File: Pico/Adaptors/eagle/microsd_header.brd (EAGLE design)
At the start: 39.3 x 17.8 mm, 3 parts

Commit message: minor board tweaks
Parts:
- R1: value (none) -> 100k
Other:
- board text added: "Pico this side"
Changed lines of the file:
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@@
 <text x="19.05" y="6.35" size="1.4224" layer="26" rot="MR0">Espruino Pico
 MicroSD rev 1.0</text>
+<text x="2.54" y="12.7" size="1.016" layer="25">Pico this side</text>
 </plain>
 <attributes>
@@
 <elements>
 <element name="J1" library="OPL Eagle Library" package="9P-SMD-W/-RING" value="" x="24.13" y="8.89"/>
-<element name="R1" library="rcl" package="R1206" value="" x="20.32" y="11.43"/>
+<element name="R1" library="rcl" package="R1206" value="100k" x="20.32" y="11.43" smashed="yes">
+<attribute name="NAME" x="19.05" y="12.7" size="1.27" layer="25"/>
+</element>
 <element name="U$1" library="espruino_pico" package="ESPRUINO_PICO_0.1" value="ESPRUINO_PICO_0.1" x="13.97" y="8.89"/>
 </elements>

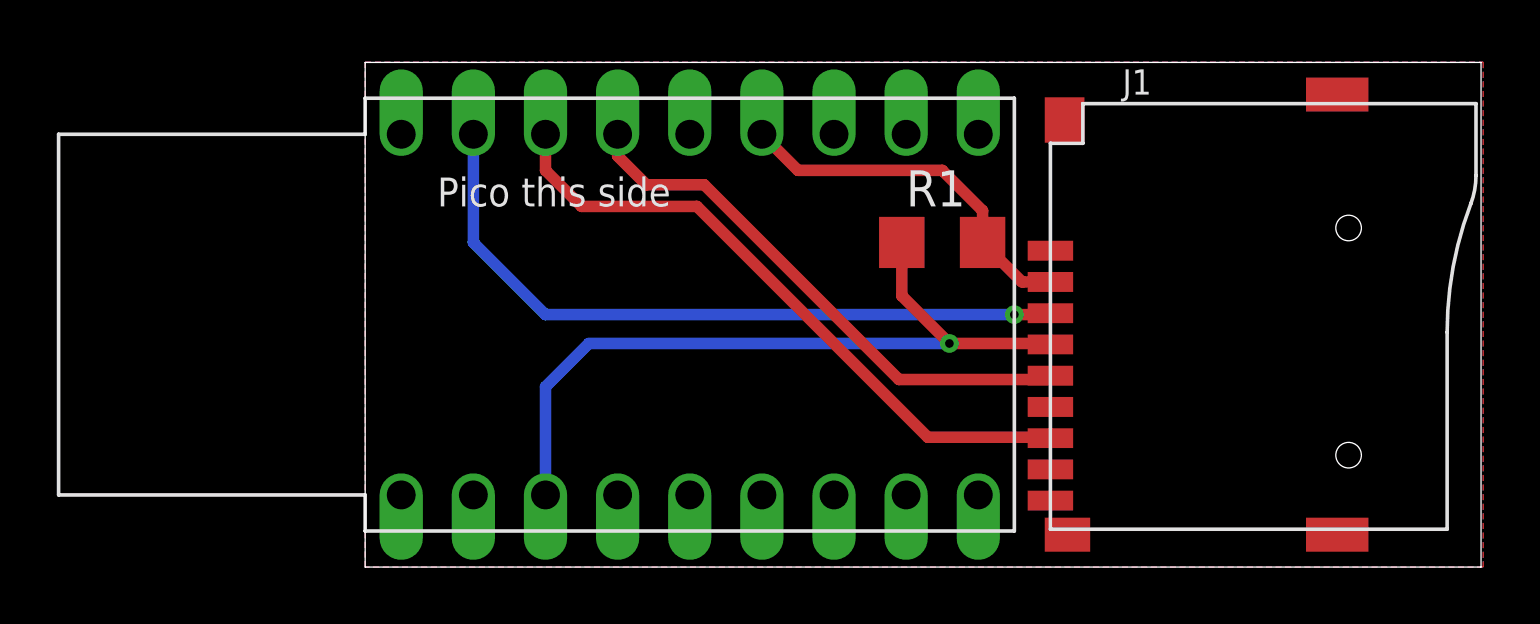
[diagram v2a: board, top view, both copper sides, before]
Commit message: fixes for SD card adaptor
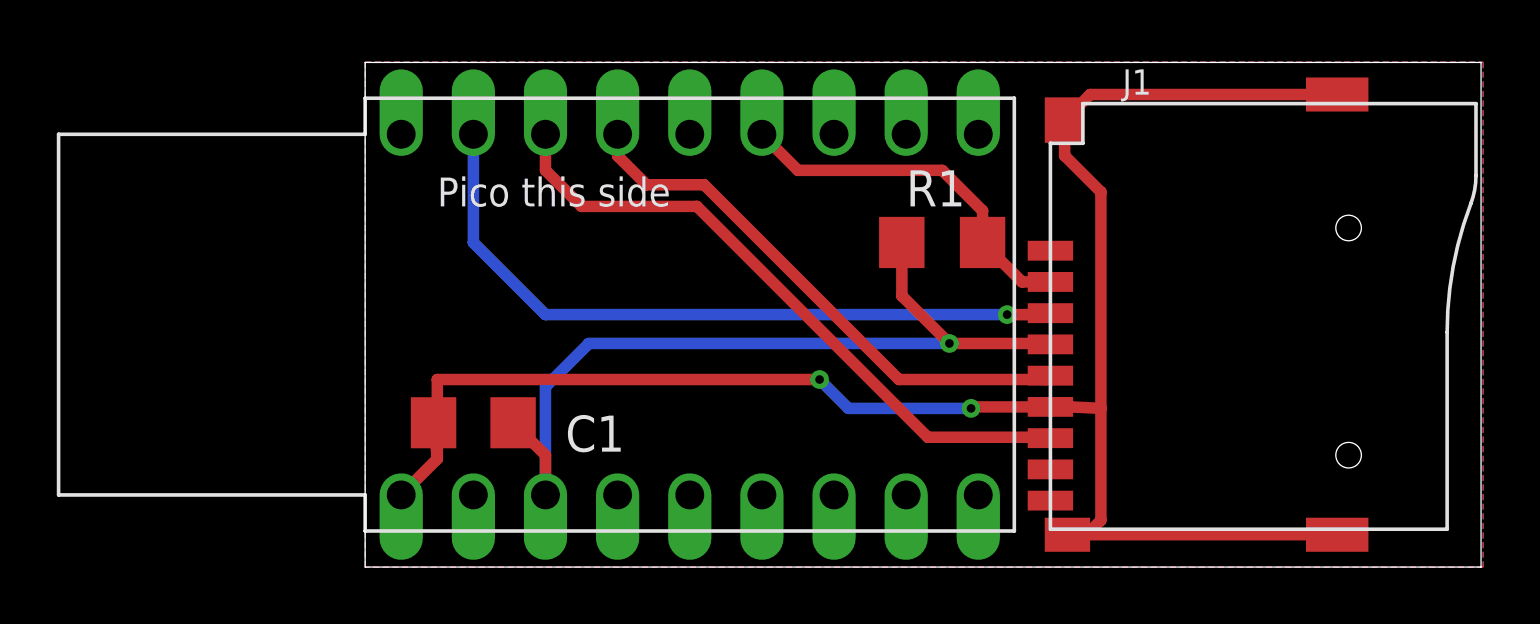
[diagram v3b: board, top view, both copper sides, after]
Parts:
- added C1: 0.1uF, rcl:C1206
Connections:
- removed net N$2: U$1.GND
- new net GND: C1.2, J1.6, J1.G1, J1.G2, J1.G3, J1.G4, U$1.GND
- net 3.3V: now also C1.1
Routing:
- net GND: track 0.00 -> 64.8 mm, vias 0 -> 2
- net 3.3V: track 26.5 -> 29.5 mm
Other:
- board text added: "Espruino Pico MicroSD rev 1.1"
- board text removed: "Espruino Pico MicroSD rev 1.0"
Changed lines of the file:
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@@
 <layers>
 <layer number="1" name="Top" color="4" fill="1" visible="yes" active="yes"/>
+<layer number="2" name="Route2" color="1" fill="3" visible="no" active="no"/>
+<layer number="15" name="Route15" color="4" fill="6" visible="no" active="no"/>
 <layer number="16" name="Bottom" color="1" fill="1" visible="yes" active="yes"/>
 <layer number="17" name="Pads" color="2" fill="1" visible="yes" active="yes"/>
@@
 CS   B1</text>
 <text x="19.05" y="6.35" size="1.4224" layer="26" rot="MR0">Espruino Pico
-MicroSD rev 1.0</text>
+MicroSD rev 1.1</text>
 <text x="2.54" y="12.7" size="1.016" layer="25">Pico this side</text>
 </plain>
@@
 </element>
 <element name="U$1" library="espruino_pico" package="ESPRUINO_PICO_0.1" value="ESPRUINO_PICO_0.1" x="13.97" y="8.89"/>
+<element name="C1" library="rcl" package="C1206" value="0.1uF" x="3.81" y="5.08" smashed="yes" rot="R180">
+<attribute name="NAME" x="9.144" y="5.334" size="1.27" layer="25" rot="R180"/>
+<attribute name="VALUE" x="6.858" y="7.62" size="1.27" layer="27" rot="R180"/>
+</element>
 </elements>
 <signals>
 <signal name="3.3V">
 <contactref element="J1" pad="4"/>
-<contactref element="R1" pad="1"/>
 <contactref element="U$1" pad="3.3V"/>
 <wire x1="24.13" y1="7.84" x2="24.096" y2="7.874" width="0.4064" layer="1"/>
-<wire x1="20.574" y1="7.874" x2="18.898" y2="9.55" width="0.4064" layer="1"/>
-<wire x1="18.898" y1="9.55" x2="18.898" y2="11.43" width="0.4064" layer="1"/>
 <wire x1="6.35" y1="2.54" x2="6.35" y2="6.35" width="0.4064" layer="16"/>
 <wire x1="6.35" y1="6.35" x2="7.874" y2="7.874" width="0.4064" layer="16"/>
@@
 <wire x1="20.574" y1="7.874" x2="24.096" y2="7.874" width="0.4064" layer="1"/>
 <via x="20.574" y="7.874" extent="1-16" drill="0.3048"/>
+<contactref element="C1" pad="1"/>
+<wire x1="6.35" y1="2.54" x2="6.35" y2="3.94" width="0.4064" layer="1"/>
+<wire x1="6.35" y1="3.94" x2="5.21" y2="5.08" width="0.4064" layer="1"/>
+<contactref element="R1" pad="1"/>
+<wire x1="18.898" y1="11.43" x2="18.898" y2="9.55" width="0.4064" layer="1"/>
+<wire x1="18.898" y1="9.55" x2="20.574" y2="7.874" width="0.4064" layer="1"/>
 </signal>
 <signal name="MOSI">
@@
 <contactref element="U$1" pad="B15"/>
 <wire x1="24.13" y1="8.94" x2="24.08" y2="8.89" width="0.4064" layer="1"/>
-<wire x1="24.08" y1="8.89" x2="22.86" y2="8.89" width="0.4064" layer="1"/>
-<via x="22.86" y="8.89" extent="1-16" drill="0.3048"/>
-<wire x1="22.86" y1="8.89" x2="6.35" y2="8.89" width="0.4064" layer="16"/>
+<wire x1="24.08" y1="8.89" x2="22.606" y2="8.89" width="0.4064" layer="1"/>
+<via x="22.606" y="8.89" extent="1-16" drill="0.3048"/>
+<wire x1="22.606" y1="8.89" x2="6.35" y2="8.89" width="0.4064" layer="16"/>
 <wire x1="6.35" y1="8.89" x2="3.81" y2="11.43" width="0.4064" layer="16"/>
 <wire x1="3.81" y1="11.43" x2="3.81" y2="15.24" width="0.4064" layer="16"/>
@@
 <contactref element="R1" pad="2"/>
 <contactref element="U$1" pad="B1"/>
+<wire x1="21.742" y1="12.548" x2="21.742" y2="11.43" width="0.4064" layer="1"/>
+<wire x1="21.742" y1="11.43" x2="23.132" y2="10.04" width="0.4064" layer="1"/>
+<wire x1="23.132" y1="10.04" x2="24.13" y2="10.04" width="0.4064" layer="1"/>
 <wire x1="13.97" y1="15.24" x2="15.24" y2="13.97" width="0.4064" layer="1"/>
 <wire x1="15.24" y1="13.97" x2="20.32" y2="13.97" width="0.4064" layer="1"/>
 <wire x1="20.32" y1="13.97" x2="21.742" y2="12.548" width="0.4064" layer="1"/>
-<wire x1="21.742" y1="12.548" x2="21.742" y2="11.43" width="0.4064" layer="1"/>
-<wire x1="21.742" y1="11.43" x2="23.132" y2="10.04" width="0.4064" layer="1"/>
-<wire x1="23.132" y1="10.04" x2="24.13" y2="10.04" width="0.4064" layer="1"/>
-</signal>
-<signal name="N$2">
-<contactref element="U$1" pad="GND"/>
 </signal>
 <signal name="GND">
@@
 <vertex x="0" y="0"/>
 </polygon>
+<contactref element="U$1" pad="GND"/>
+<contactref element="J1" pad="6"/>
+<wire x1="24.13" y1="5.64" x2="21.336" y2="5.64" width="0.4064" layer="1"/>
+<wire x1="21.336" y1="5.64" x2="21.336" y2="5.588" width="0.4064" layer="1"/>
+<via x="21.336" y="5.588" extent="1-16" drill="0.3048"/>
+<wire x1="21.336" y1="5.588" x2="17.018" y2="5.588" width="0.4064" layer="16"/>
+<wire x1="17.018" y1="5.588" x2="16.002" y2="6.604" width="0.4064" layer="16"/>
+<via x="16.002" y="6.604" extent="1-16" drill="0.3048"/>
+<wire x1="16.002" y1="6.604" x2="2.54" y2="6.604" width="0.4064" layer="1"/>
+<wire x1="2.54" y1="6.604" x2="2.54" y2="3.81" width="0.4064" layer="1"/>
+<wire x1="2.54" y1="3.81" x2="1.27" y2="2.54" width="0.4064" layer="1"/>
+<contactref element="J1" pad="G4"/>
+<contactref element="J1" pad="G3"/>
+<contactref element="J1" pad="G1"/>
+<contactref element="J1" pad="G2"/>
+<wire x1="34.23" y1="16.64" x2="25.53" y2="16.64" width="0.4064" layer="1"/>
+<wire x1="25.53" y1="16.64" x2="24.63" y2="15.74" width="0.4064" layer="1"/>
+<wire x1="24.73" y1="1.14" x2="25.4" y2="1.14" width="0.4064" layer="1"/>
+<wire x1="25.4" y1="1.14" x2="34.23" y2="1.14" width="0.4064" layer="1"/>
+<wire x1="24.13" y1="5.64" x2="24.84" y2="5.64" width="0.4064" layer="1"/>
+<wire x1="24.84" y1="5.64" x2="25.908" y2="5.588" width="0.4064" layer="1"/>
+<wire x1="25.908" y1="5.588" x2="25.908" y2="1.648" width="0.4064" layer="1"/>
+<wire x1="25.908" y1="1.648" x2="25.4" y2="1.14" width="0.4064" layer="1"/>
+<wire x1="24.63" y1="15.74" x2="24.63" y2="14.486" width="0.4064" layer="1"/>
+<wire x1="24.63" y1="14.486" x2="25.908" y2="13.208" width="0.4064" layer="1"/>
+<wire x1="25.908" y1="13.208" x2="25.908" y2="5.588" width="0.4064" layer="1"/>
+<contactref element="C1" pad="2"/>
+<wire x1="2.41" y1="5.08" x2="2.41" y2="5.21" width="0.4064" layer="1"/>
+<wire x1="2.41" y1="5.21" x2="2.54" y2="3.81" width="0.4064" layer="1"/>
 </signal>
 </signals>
